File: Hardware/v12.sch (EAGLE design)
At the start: 82 parts, among them IC1 LM324D, IC2 m328p, IC3 REG1117, IC4 OPA336U, J1 22-27-2081-08, J2 22-27-2031-03

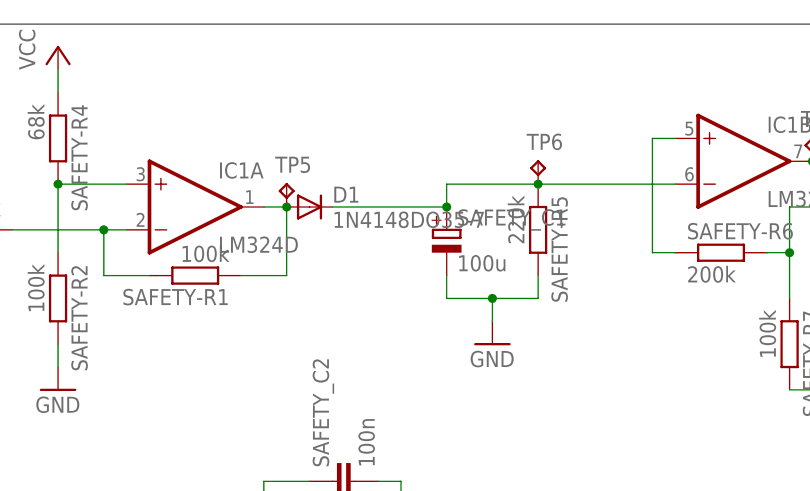
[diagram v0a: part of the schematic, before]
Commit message: changed diode to a minimelf diode from open parts library
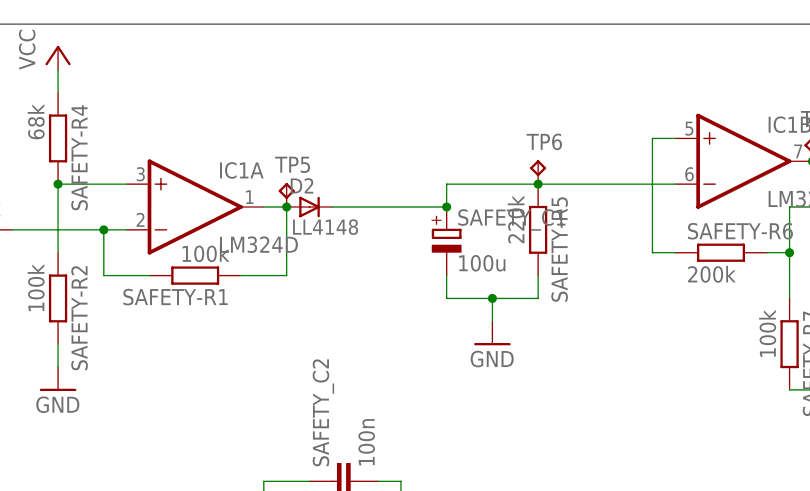
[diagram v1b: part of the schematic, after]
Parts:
- removed D1: 1N4148DO35-7, diode:1N4148DO35-7
- added D2: LL4148, _hhn_diodes_smd:LL4148
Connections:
- net N$11: now also D2.C; no longer D1.C
- net N$7: now also D2.A; no longer D1.A
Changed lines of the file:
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@@
 <part name="GND16" library="supply1" deviceset="GND" device=""/>
 <part name="P+11" library="supply1" deviceset="VCC" device=""/>
-<part name="D1" library="diode" deviceset="1N4148" device="DO35-7"/>
 <part name="SAFETY_C1" library="rcl" deviceset="CPOL-EU" device="E2-5" value="100u"/>
 <part name="SAFETY-R5" library="rcl" deviceset="R-EU_" device="R0603" value="220k"/>
@@
 <part name="TP6" library="testpad" deviceset="TP" device="B1,27"/>
 <part name="TP7" library="testpad" deviceset="TP" device="B1,27"/>
+<part name="D2" library="_hhn_diodes_smd" deviceset="LL4148" device=""/>
 </parts>
 <sheets>
@@
 <instance part="GND16" gate="1" x="266.7" y="220.98"/>
 <instance part="P+11" gate="VCC" x="266.7" y="259.08"/>
-<instance part="D1" gate="G$1" x="294.64" y="241.3"/>
 <instance part="SAFETY_C1" gate="G$1" x="309.88" y="238.76"/>
 <instance part="SAFETY-R5" gate="G$1" x="320.04" y="238.76" rot="R270"/>
@@
 <instance part="TP6" gate="G$1" x="320.04" y="246.38"/>
 <instance part="TP7" gate="G$1" x="350.52" y="248.92"/>
+<instance part="D2" gate="G$1" x="294.64" y="241.3"/>
 </instances>
 <busses>
@@
 <pinref part="SAFETY-R1" gate="G$1" pin="1"/>
 <wire x1="287.02" y1="233.68" x2="292.1" y2="233.68" width="0.1524" layer="91"/>
-<pinref part="D1" gate="G$1" pin="A"/>
 <junction x="292.1" y="241.3"/>
 <pinref part="TP5" gate="G$1" pin="TP"/>
+<pinref part="D2" gate="G$1" pin="A"/>
 </segment>
 </net>
@@
 <net name="N$11" class="0">
 <segment>
-<pinref part="D1" gate="G$1" pin="C"/>
 <pinref part="SAFETY_C1" gate="G$1" pin="+"/>
 <wire x1="297.18" y1="241.3" x2="309.88" y2="241.3" width="0.1524" layer="91"/>
@@
 <wire x1="320.04" y1="243.84" x2="335.28" y2="243.84" width="0.1524" layer="91"/>
 <pinref part="TP6" gate="G$1" pin="TP"/>
-</segment>
-</net>
+<pinref part="D2" gate="G$1" pin="C"/>
+</segment>
+</net>

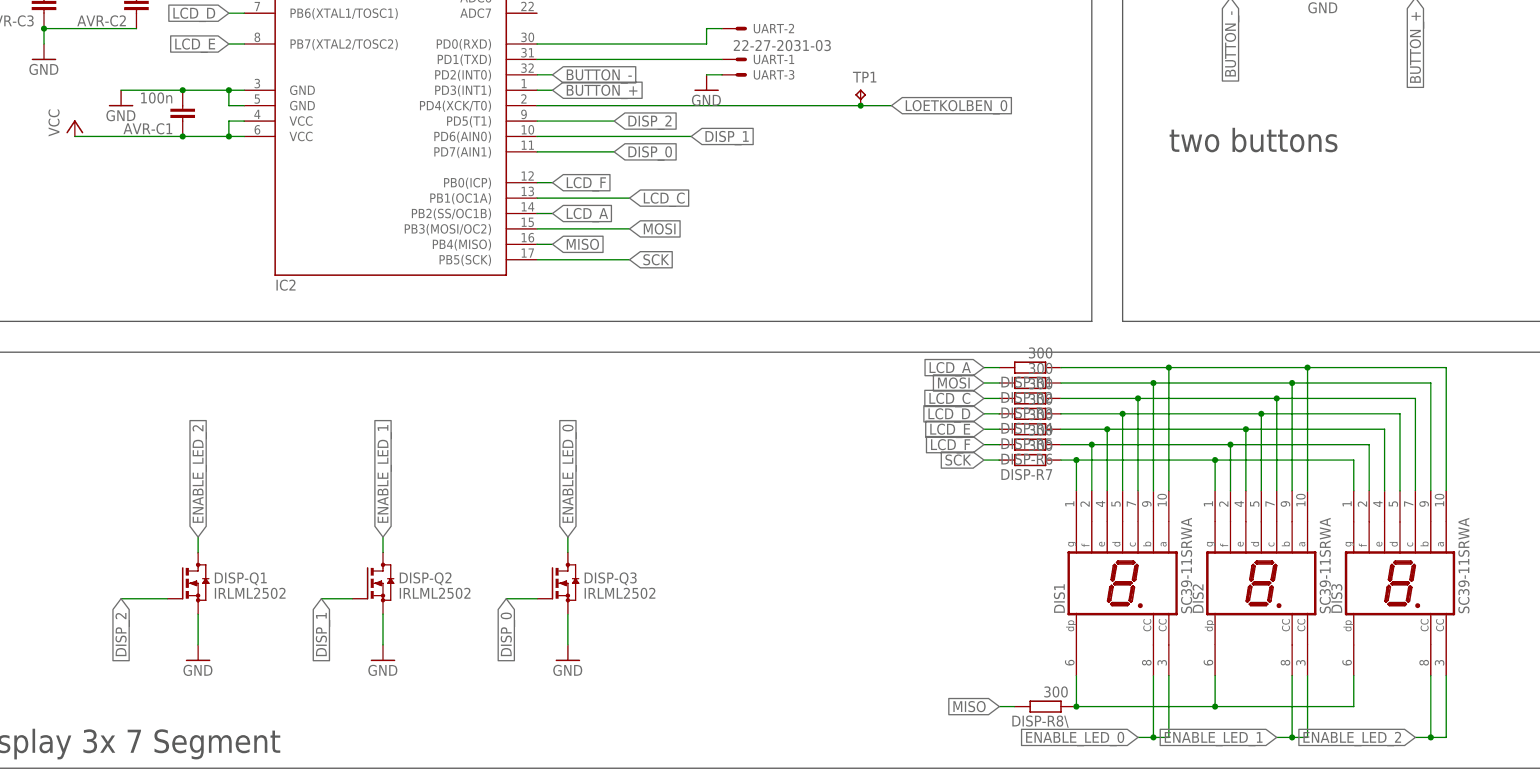
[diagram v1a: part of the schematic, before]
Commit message: slight renaming for better understanding
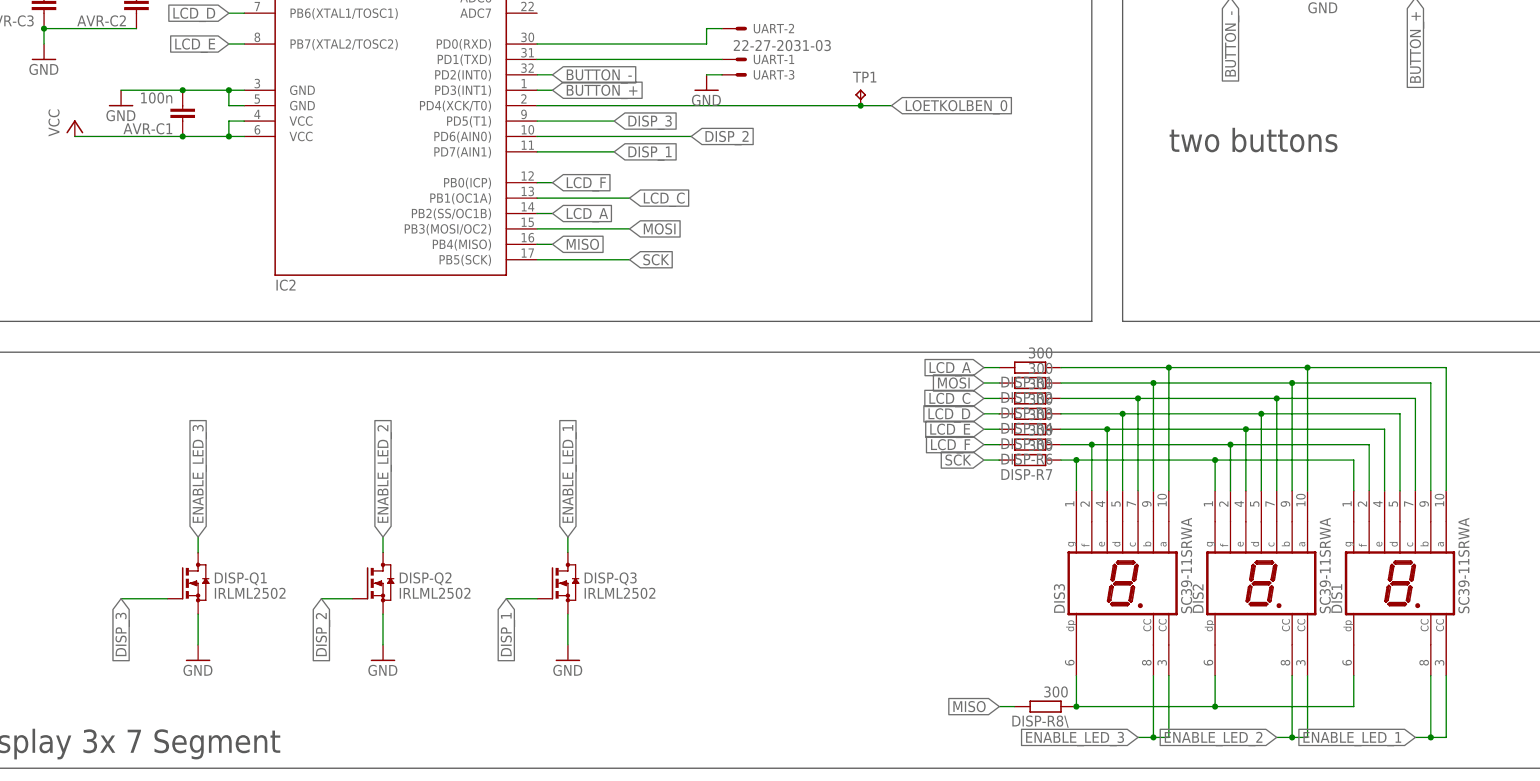
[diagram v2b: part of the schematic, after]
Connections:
- removed net DISP_0: DISP-Q3.G, IC2.PD7(AIN1)
- removed net ENABLE_LED_0: DIS1.CC, DIS1.CC@1, DISP-Q3.D
- new net DISP_3: DISP-Q1.G, IC2.PD5(T1)
- new net ENABLE_LED_3: DIS3.CC, DIS3.CC@1, DISP-Q1.D
- net DISP_1: now also DISP-Q3.G, IC2.PD7(AIN1); no longer DISP-Q2.G, IC2.PD6(AIN0)
- net DISP_2: now also DISP-Q2.G, IC2.PD6(AIN0); no longer DISP-Q1.G, IC2.PD5(T1)
- net ENABLE_LED_1: now also DIS1.CC, DIS1.CC@1, DISP-Q3.D; no longer DIS2.CC, DIS2.CC@1, DISP-Q2.D
- net ENABLE_LED_2: now also DIS2.CC, DIS2.CC@1, DISP-Q2.D; no longer DIS3.CC, DIS3.CC@1, DISP-Q1.D
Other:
- moved on the sheet: DIS1, DIS3
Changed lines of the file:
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@@
 <instance part="P+10" gate="VCC" x="223.52" y="182.88"/>
 <instance part="DIS2" gate="G$1" x="322.58" y="58.42"/>
-<instance part="DIS1" gate="G$1" x="299.72" y="58.42"/>
-<instance part="DIS3" gate="G$1" x="345.44" y="58.42"/>
+<instance part="DIS1" gate="G$1" x="345.44" y="58.42"/>
+<instance part="DIS3" gate="G$1" x="299.72" y="58.42"/>
 <instance part="DISP-R7" gate="G$1" x="284.48" y="78.74" rot="R180"/>
 <instance part="DISP-R6" gate="G$1" x="284.48" y="81.28" rot="R180"/>
@@
 </segment>
 </net>
-<net name="ENABLE_LED_1" class="0">
+<net name="ENABLE_LED_2" class="0">
 <segment>
 <pinref part="DISP-Q2" gate="G$1" pin="D"/>
@@
 </segment>
 </net>
-<net name="ENABLE_LED_2" class="0">
+<net name="ENABLE_LED_3" class="0">
 <segment>
 <pinref part="DISP-Q1" gate="G$1" pin="D"/>
@@
 <segment>
 <pinref part="DIS3" gate="G$1" pin="CC"/>
-<wire x1="350.52" y1="33.02" x2="350.52" y2="43.18" width="0.1524" layer="91"/>
+<wire x1="304.8" y1="33.02" x2="304.8" y2="43.18" width="0.1524" layer="91"/>
 <pinref part="DIS3" gate="G$1" pin="CC@1"/>
-<wire x1="350.52" y1="33.02" x2="353.06" y2="33.02" width="0.1524" layer="91"/>
-<wire x1="353.06" y1="33.02" x2="353.06" y2="43.18" width="0.1524" layer="91"/>
-<wire x1="347.98" y1="33.02" x2="350.52" y2="33.02" width="0.1524" layer="91"/>
-<junction x="350.52" y="33.02"/>
-<label x="347.98" y="33.02" size="1.778" layer="95" rot="R180" xref="yes"/>
-</segment>
-</net>
-<net name="ENABLE_LED_0" class="0">
+<wire x1="304.8" y1="33.02" x2="307.34" y2="33.02" width="0.1524" layer="91"/>
+<wire x1="307.34" y1="33.02" x2="307.34" y2="43.18" width="0.1524" layer="91"/>
+<wire x1="302.26" y1="33.02" x2="304.8" y2="33.02" width="0.1524" layer="91"/>
+<junction x="304.8" y="33.02"/>
+<label x="302.26" y="33.02" size="1.778" layer="95" rot="R180" xref="yes"/>
+</segment>
+</net>
+<net name="ENABLE_LED_1" class="0">
 <segment>
 <pinref part="DISP-Q3" gate="G$1" pin="D"/>
@@
 <segment>
 <pinref part="DIS1" gate="G$1" pin="CC@1"/>
-<wire x1="307.34" y1="33.02" x2="307.34" y2="43.18" width="0.1524" layer="91"/>
+<wire x1="353.06" y1="33.02" x2="353.06" y2="43.18" width="0.1524" layer="91"/>
 <pinref part="DIS1" gate="G$1" pin="CC"/>
-<wire x1="304.8" y1="43.18" x2="304.8" y2="33.02" width="0.1524" layer="91"/>
-<wire x1="304.8" y1="33.02" x2="307.34" y2="33.02" width="0.1524" layer="91"/>
-<wire x1="304.8" y1="33.02" x2="302.26" y2="33.02" width="0.1524" layer="91"/>
-<junction x="304.8" y="33.02"/>
-<label x="302.26" y="33.02" size="1.778" layer="95" rot="R180" xref="yes"/>
+<wire x1="350.52" y1="43.18" x2="350.52" y2="33.02" width="0.1524" layer="91"/>
+<wire x1="350.52" y1="33.02" x2="353.06" y2="33.02" width="0.1524" layer="91"/>
+<wire x1="350.52" y1="33.02" x2="347.98" y2="33.02" width="0.1524" layer="91"/>
+<junction x="350.52" y="33.02"/>
+<label x="347.98" y="33.02" size="1.778" layer="95" rot="R180" xref="yes"/>
 </segment>
 </net>
@@
 </segment>
 </net>
-<net name="DISP_0" class="0">
+<net name="DISP_1" class="0">
 <segment>
 <pinref part="DISP-Q3" gate="G$1" pin="G"/>
@@
 </segment>
 </net>
-<net name="DISP_2" class="0">
+<net name="DISP_3" class="0">
 <segment>
 <pinref part="DISP-Q1" gate="G$1" pin="G"/>
@@
 </segment>
 </net>
-<net name="DISP_1" class="0">
+<net name="DISP_2" class="0">
 <segment>
 <pinref part="DISP-Q2" gate="G$1" pin="G"/>
@@
 <segment>
 <pinref part="DIS1" gate="G$1" pin="DP"/>
-<wire x1="292.1" y1="43.18" x2="292.1" y2="38.1" width="0.1524" layer="91"/>
 <pinref part="DIS2" gate="G$1" pin="DP"/>
 <wire x1="292.1" y1="38.1" x2="314.96" y2="38.1" width="0.1524" layer="91"/>
@@
 <pinref part="DIS3" gate="G$1" pin="DP"/>
 <wire x1="314.96" y1="38.1" x2="337.82" y2="38.1" width="0.1524" layer="91"/>
-<wire x1="337.82" y1="38.1" x2="337.82" y2="43.18" width="0.1524" layer="91"/>
 <junction x="314.96" y="38.1"/>
 <pinref part="DISP-R8\" gate="G$1" pin="1"/>
 <junction x="292.1" y="38.1"/>
+<wire x1="292.1" y1="43.18" x2="292.1" y2="38.1" width="0.1524" layer="91"/>
+<wire x1="337.82" y1="43.18" x2="337.82" y2="38.1" width="0.1524" layer="91"/>
 </segment>
 </net>
@@
 <segment>
 <pinref part="DIS1" gate="G$1" pin="E"/>
-<wire x1="297.18" y1="73.66" x2="297.18" y2="83.82" width="0.1524" layer="91"/>
 <pinref part="DIS2" gate="G$1" pin="E"/>
 <wire x1="297.18" y1="83.82" x2="320.04" y2="83.82" width="0.1524" layer="91"/>
@@
 <pinref part="DIS3" gate="G$1" pin="E"/>
 <wire x1="320.04" y1="83.82" x2="342.9" y2="83.82" width="0.1524" layer="91"/>
-<wire x1="342.9" y1="83.82" x2="342.9" y2="73.66" width="0.1524" layer="91"/>
 <junction x="320.04" y="83.82"/>
 <pinref part="DISP-R5" gate="G$1" pin="1"/>
 <wire x1="297.18" y1="83.82" x2="289.56" y2="83.82" width="0.1524" layer="91"/>
 <junction x="297.18" y="83.82"/>
+<wire x1="342.9" y1="83.82" x2="342.9" y2="73.66" width="0.1524" layer="91"/>
+<wire x1="297.18" y1="83.82" x2="297.18" y2="73.66" width="0.1524" layer="91"/>
 </segment>
 </net>
@@
 <segment>
 <pinref part="DIS1" gate="G$1" pin="D"/>
-<wire x1="299.72" y1="73.66" x2="299.72" y2="86.36" width="0.1524" layer="91"/>
 <pinref part="DIS2" gate="G$1" pin="D"/>
 <wire x1="299.72" y1="86.36" x2="322.58" y2="86.36" width="0.1524" layer="91"/>
@@
 <pinref part="DIS3" gate="G$1" pin="D"/>
 <wire x1="322.58" y1="86.36" x2="345.44" y2="86.36" width="0.1524" layer="91"/>
-<wire x1="345.44" y1="86.36" x2="345.44" y2="73.66" width="0.1524" layer="91"/>
 <junction x="322.58" y="86.36"/>
 <pinref part="DISP-R4" gate="G$1" pin="1"/>
 <wire x1="289.56" y1="86.36" x2="299.72" y2="86.36" width="0.1524" layer="91"/>
 <junction x="299.72" y="86.36"/>
+<wire x1="345.44" y1="73.66" x2="345.44" y2="86.36" width="0.1524" layer="91"/>
+<wire x1="299.72" y1="73.66" x2="299.72" y2="86.36" width="0.1524" layer="91"/>
 </segment>
 </net>
@@
 <segment>
 <pinref part="DIS1" gate="G$1" pin="C"/>
-<wire x1="302.26" y1="73.66" x2="302.26" y2="88.9" width="0.1524" layer="91"/>
 <pinref part="DIS2" gate="G$1" pin="C"/>
 <wire x1="302.26" y1="88.9" x2="325.12" y2="88.9" width="0.1524" layer="91"/>
@@
 <pinref part="DIS3" gate="G$1" pin="C"/>
 <wire x1="325.12" y1="88.9" x2="347.98" y2="88.9" width="0.1524" layer="91"/>
-<wire x1="347.98" y1="88.9" x2="347.98" y2="73.66" width="0.1524" layer="91"/>
 <junction x="325.12" y="88.9"/>
 <pinref part="DISP-R3" gate="G$1" pin="1"/>
 <wire x1="302.26" y1="88.9" x2="289.56" y2="88.9" width="0.1524" layer="91"/>
 <junction x="302.26" y="88.9"/>
+<wire x1="347.98" y1="88.9" x2="347.98" y2="73.66" width="0.1524" layer="91"/>
+<wire x1="302.26" y1="88.9" x2="302.26" y2="73.66" width="0.1524" layer="91"/>
 </segment>
 </net>
@@
 <segment>
 <pinref part="DIS3" gate="G$1" pin="B"/>
-<wire x1="350.52" y1="73.66" x2="350.52" y2="91.44" width="0.1524" layer="91"/>
 <pinref part="DIS2" gate="G$1" pin="B"/>
 <wire x1="350.52" y1="91.44" x2="327.66" y2="91.44" width="0.1524" layer="91"/>
@@
 <pinref part="DIS1" gate="G$1" pin="B"/>
 <wire x1="327.66" y1="91.44" x2="304.8" y2="91.44" width="0.1524" layer="91"/>
-<wire x1="304.8" y1="91.44" x2="304.8" y2="73.66" width="0.1524" layer="91"/>
 <junction x="327.66" y="91.44"/>
 <pinref part="DISP-R2" gate="G$1" pin="1"/>
 <wire x1="289.56" y1="91.44" x2="304.8" y2="91.44" width="0.1524" layer="91"/>
 <junction x="304.8" y="91.44"/>
+<wire x1="350.52" y1="73.66" x2="350.52" y2="91.44" width="0.1524" layer="91"/>
+<wire x1="304.8" y1="73.66" x2="304.8" y2="91.44" width="0.1524" layer="91"/>
 </segment>
 </net>
@@
 <segment>
 <pinref part="DIS1" gate="G$1" pin="A"/>
-<wire x1="307.34" y1="73.66" x2="307.34" y2="93.98" width="0.1524" layer="91"/>
 <pinref part="DIS2" gate="G$1" pin="A"/>
 <wire x1="307.34" y1="93.98" x2="330.2" y2="93.98" width="0.1524" layer="91"/>
@@
 <pinref part="DIS3" gate="G$1" pin="A"/>
 <wire x1="330.2" y1="93.98" x2="353.06" y2="93.98" width="0.1524" layer="91"/>
-<wire x1="353.06" y1="93.98" x2="353.06" y2="73.66" width="0.1524" layer="91"/>
 <junction x="330.2" y="93.98"/>
 <pinref part="DISP-R1" gate="G$1" pin="1"/>
 <wire x1="307.34" y1="93.98" x2="289.56" y2="93.98" width="0.1524" layer="91"/>
 <junction x="307.34" y="93.98"/>
+<wire x1="353.06" y1="93.98" x2="353.06" y2="73.66" width="0.1524" layer="91"/>
+<wire x1="307.34" y1="93.98" x2="307.34" y2="73.66" width="0.1524" layer="91"/>
 </segment>
 </net>
@@
 <segment>
 <pinref part="DIS1" gate="G$1" pin="F"/>
-<wire x1="294.64" y1="73.66" x2="294.64" y2="81.28" width="0.1524" layer="91"/>
 <pinref part="DIS2" gate="G$1" pin="F"/>
 <wire x1="294.64" y1="81.28" x2="317.5" y2="81.28" width="0.1524" layer="91"/>
@@
 <pinref part="DIS3" gate="G$1" pin="F"/>
 <wire x1="317.5" y1="81.28" x2="340.36" y2="81.28" width="0.1524" layer="91"/>
-<wire x1="340.36" y1="81.28" x2="340.36" y2="73.66" width="0.1524" layer="91"/>
 <junction x="317.5" y="81.28"/>
 <pinref part="DISP-R6" gate="G$1" pin="1"/>
 <wire x1="289.56" y1="81.28" x2="294.64" y2="81.28" width="0.1524" layer="91"/>
 <junction x="294.64" y="81.28"/>
+<wire x1="340.36" y1="73.66" x2="340.36" y2="81.28" width="0.1524" layer="91"/>
+<wire x1="294.64" y1="73.66" x2="294.64" y2="81.28" width="0.1524" layer="91"/>
 </segment>
 </net>
@@
 <segment>
 <pinref part="DIS3" gate="G$1" pin="G"/>
-<wire x1="337.82" y1="73.66" x2="337.82" y2="78.74" width="0.1524" layer="91"/>
 <pinref part="DIS2" gate="G$1" pin="G"/>
 <wire x1="337.82" y1="78.74" x2="314.96" y2="78.74" width="0.1524" layer="91"/>
@@
 <pinref part="DIS1" gate="G$1" pin="G"/>
 <wire x1="314.96" y1="78.74" x2="292.1" y2="78.74" width="0.1524" layer="91"/>
-<wire x1="292.1" y1="78.74" x2="292.1" y2="73.66" width="0.1524" layer="91"/>
 <junction x="314.96" y="78.74"/>
 <pinref part="DISP-R7" gate="G$1" pin="1"/>
 <wire x1="292.1" y1="78.74" x2="289.56" y2="78.74" width="0.1524" layer="91"/>
 <junction x="292.1" y="78.74"/>
-</segment>
-</net>
+<wire x1="337.82" y1="78.74" x2="337.82" y2="73.66" width="0.1524" layer="91"/>
+<wire x1="292.1" y1="78.74" x2="292.1" y2="73.66" width="0.1524" layer="91"/>
+</segment>
+</net>
